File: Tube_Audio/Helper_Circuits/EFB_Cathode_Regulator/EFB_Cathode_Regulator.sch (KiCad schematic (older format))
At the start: 9 parts, among them J1 Screw_Terminal_01x03, J2 Screw_Terminal_01x02, U1 LM337_TO220

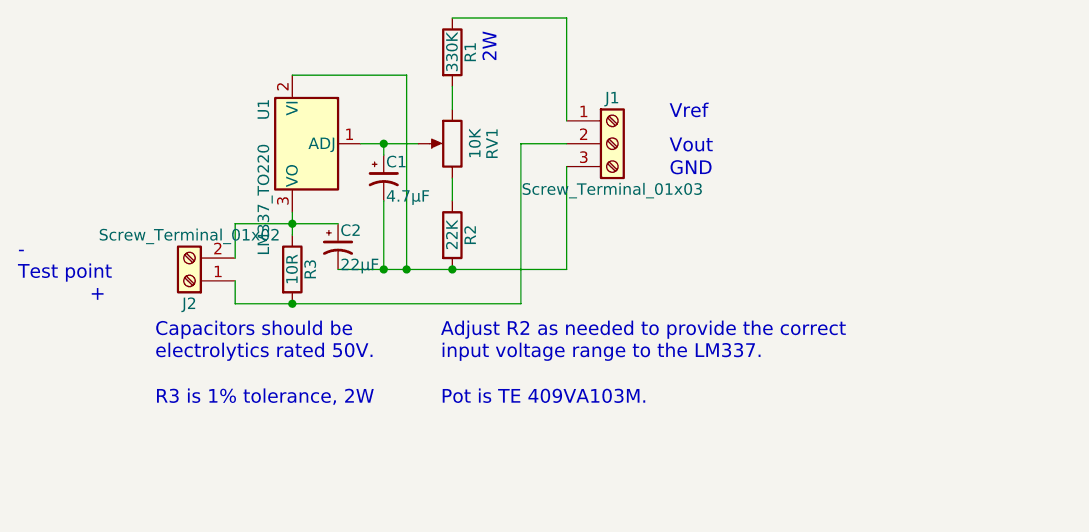
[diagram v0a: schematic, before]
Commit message: Clarify trademark status in all materials.
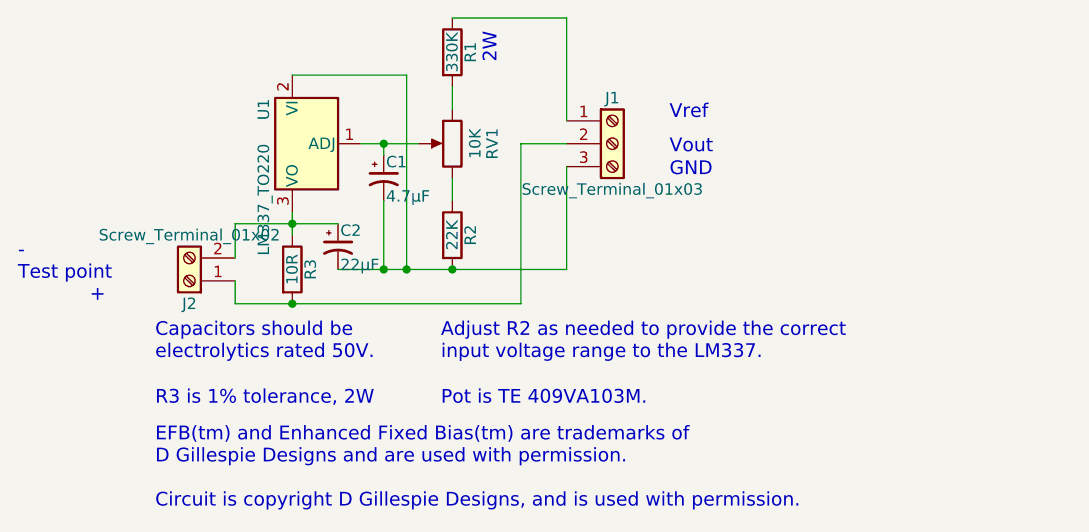
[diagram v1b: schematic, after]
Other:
- note added: "EFB(tm) and Enhanced Fixed Bias(tm) are trademarks of\nD Gillespie Designs and are used with permission.\n\nCircuit is copyright D Gillespie Designs, and is used with permission."
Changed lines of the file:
@@
 LIBS:contrib
 LIBS:valves
+LIBS:EFB_Cathode_Regulator-cache
 EELAYER 25 0
 EELAYER END
@@
 Text Notes 5250 4550 0    60   ~ 0
 R3 is 1% tolerance, 2W
+Text Notes 5250 5000 0    60   ~ 0
+EFB(tm) and Enhanced Fixed Bias(tm) are trademarks of\nD Gillespie Designs and are used with permission.\n\nCircuit is copyright D Gillespie Designs, and is used with permission.
 $EndSCHEMATC
